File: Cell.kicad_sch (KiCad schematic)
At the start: 19 parts

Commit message: Deleted '-' from its name, officially
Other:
- title: SRAM cell for RT-08 Program board -> SRAM cell for RT08 Program board
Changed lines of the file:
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@@
 	(paper "User" 208.077 65.024)
 	(title_block
-		(title "SRAM cell for RT-08 Program board")
+		(title "SRAM cell for RT08 Program board")
 		(date "2025-05-24")
 		(company "@7654jp")

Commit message: Updated pinouts n' something
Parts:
- R1, R2, R3, R4, R5: footprint YoshLibrary:R_Axial_DIN0207_L6.3mm_D2.5mm_P7.62mm_Horizontal -> YoshLibrary:R_Axial_DIN0207_L6.3mm_D2.5mm_P7.62mm_Horizontal_Y
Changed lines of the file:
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@@
 			)
 		)
-		(property "Footprint" "YoshLibrary:R_Axial_DIN0207_L6.3mm_D2.5mm_P7.62mm_Horizontal"
+		(property "Footprint" "YoshLibrary:R_Axial_DIN0207_L6.3mm_D2.5mm_P7.62mm_Horizontal_Y"
 			(at 57.15 22.86 0)
 			(effects
@@
 			)
 		)
-		(property "Footprint" "YoshLibrary:R_Axial_DIN0207_L6.3mm_D2.5mm_P7.62mm_Horizontal"
+		(property "Footprint" "YoshLibrary:R_Axial_DIN0207_L6.3mm_D2.5mm_P7.62mm_Horizontal_Y"
 			(at 59.182 44.45 90)
 			(effects
@@
 			)
 		)
-		(property "Footprint" "YoshLibrary:R_Axial_DIN0207_L6.3mm_D2.5mm_P7.62mm_Horizontal"
+		(property "Footprint" "YoshLibrary:R_Axial_DIN0207_L6.3mm_D2.5mm_P7.62mm_Horizontal_Y"
 			(at 64.77 27.94 0)
 			(effects
@@
 			)
 		)
-		(property "Footprint" "YoshLibrary:R_Axial_DIN0207_L6.3mm_D2.5mm_P7.62mm_Horizontal"
+		(property "Footprint" "YoshLibrary:R_Axial_DIN0207_L6.3mm_D2.5mm_P7.62mm_Horizontal_Y"
 			(at 50.8 27.94 0)
 			(effects
@@
 			)
 		)
-		(property "Footprint" "YoshLibrary:R_Axial_DIN0207_L6.3mm_D2.5mm_P7.62mm_Horizontal"
+		(property "Footprint" "YoshLibrary:R_Axial_DIN0207_L6.3mm_D2.5mm_P7.62mm_Horizontal_Y"
 			(at 27.178 31.75 90)
 			(effects

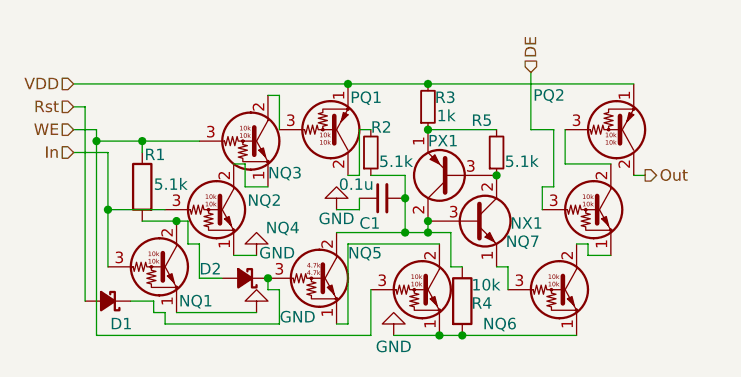
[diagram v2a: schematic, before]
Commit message: Adding one more parts per bit, editing PCB
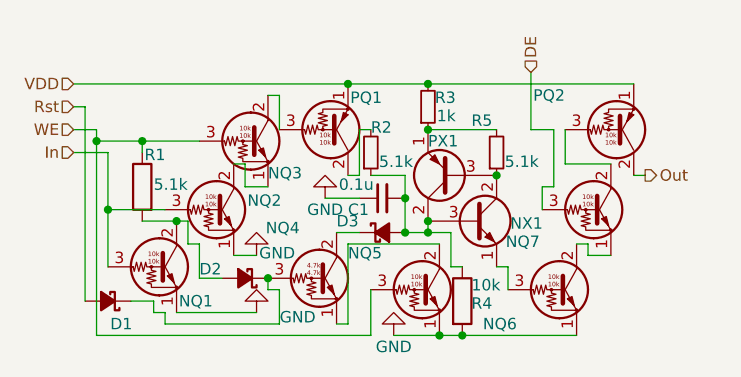
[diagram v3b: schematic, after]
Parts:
- added D3: Schottky, Diode_THT:D_DO-35_SOD27_P7.62mm_Horizontal, symbol Device:D_Schottky_Small_Filled
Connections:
- net at C1.2, NX1.3 (B), PX1.2 (C)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: now also D3.2 (A); no longer NQ4.2 (C)
- new net: D3.1 (K), NQ4.2 (C)

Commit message: Remaking due to design change, wip1
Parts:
- removed NQ6: DTC114E-THT, Package_TO_SOT_THT:TO-92_Inline_Wide, symbol YoshLibrary:DTC114E-THT
- removed R1: 5.1k, YoshLibrary:R_Axial_DIN0207_L6.3mm_D2.5mm_P7.62mm_Horizontal_Y, symbol Device:R
- removed R4: 10k, YoshLibrary:R_Axial_DIN0207_L6.3mm_D2.5mm_P7.62mm_Horizontal_Y, symbol Device:R
- added NQ6: DTC143E-THT, Package_TO_SOT_THT:TO-92_Inline_Wide, symbol YoshLibrary:DTC143E-THT
- added R1, R4: 5.1k, Resistor_THT:R_Axial_DIN0207_L6.3mm_D2.5mm_P7.62mm_Horizontal, symbol Device:R_Small
- D1, D2, D3: value Schottky -> 30V0.2A
- R2: footprint YoshLibrary:R_Axial_DIN0207_L6.3mm_D2.5mm_P7.62mm_Horizontal_Y -> Resistor_THT:R_Axial_DIN0207_L6.3mm_D2.5mm_P7.62mm_Horizontal
- R3: value 1k -> 5.1k; footprint YoshLibrary:R_Axial_DIN0207_L6.3mm_D2.5mm_P7.62mm_Horizontal_Y -> Resistor_THT:R_Axial_DIN0207_L6.3mm_D2.5mm_P7.62mm_Horizontal
- R5: value 5.1k -> 10k; footprint YoshLibrary:R_Axial_DIN0207_L6.3mm_D2.5mm_P7.62mm_Horizontal_Y -> Resistor_THT:R_Axial_DIN0207_L6.3mm_D2.5mm_P7.62mm_Horizontal
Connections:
- net DE: now also NQ3.3 (B); no longer NQ7.3 (B)
- net GND: now also NQ7.1 (E), R5.2, NQ6.1 (E); no longer NQ1.1 (E)
- net In: now also NQ5.3 (B); no longer NQ1.3 (B)
- net Rst: now also D3.2 (A), NQ6.3 (B); no longer D1.2 (A)
- net VDD: now also R1.2; no longer R3.2
- net WE: now also NQ1.3 (B), R2.2; no longer NQ3.3 (B), NQ5.3 (B)
- net at NQ4.2 (C): now also D1.1 (K); no longer D3.1 (K)
- net at C1.2, NX1.3 (B), PX1.2 (C): now also D1.2 (A), R5.1, R4.1; no longer D3.2 (A), R2.1
- net at D2.2 (A): now also NQ5.2 (C), R2.1; no longer NQ1.2 (C)
- net at NQ3.1 (E): now also NQ7.2 (C); no longer NQ2.2 (C)
- net at NQ4.1 (E): now also NQ6.2 (C); no longer NQ5.2 (C)
- net at D2.1 (K), NQ4.3 (B): now also D3.1 (K); no longer D1.1 (K)
- net at NQ3.2 (C): now also PQ2.3 (B); no longer PQ1.3 (B)
- net at NX1.1 (E): now also NQ7.3 (B)
- net at NX1.2 (C), PX1.3 (B): now also R3.1; no longer R5.1
- net at PQ1.2 (C): now also R4.2; no longer R2.2
- new net: NQ1.2 (C), PQ1.3 (B)
- new net: NQ1.1 (E), NQ2.2 (C)
- new net: PX1.1 (E), R1.1, R3.2

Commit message: New design completed
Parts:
- removed D1: 30V0.2A, Diode_THT:D_DO-35_SOD27_P7.62mm_Horizontal, symbol Device:D_Schottky_Small_Filled
- removed NQ6: DTC143E-THT, Package_TO_SOT_THT:TO-92_Inline_Wide, symbol YoshLibrary:DTC143E-THT
- renumbered D2 to D1, D3 to D2, NQ5 to NQ3, NQ3 to NQ5, NQ7 to NQ6, R2 to R1, R1 to R2
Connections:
- net GND: now also NQ4.1 (E)
- net at NQ4.2 (C): now also C1.2, NX1.3 (B), PX1.2 (C), R4.1, R5.1
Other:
- moved on the sheet: C1, D1, D2, NQ1, NQ2, NQ3, NQ4, NQ5, NQ6, NX1, PQ1, PQ2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
